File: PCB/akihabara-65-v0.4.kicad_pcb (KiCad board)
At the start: 2 copper layers, 327.6 x 99 mm, 198 parts, among them J1 JST-SH, J2 SWD, Q1 2N7002, SW1 TS-1187A-B-A-B, U1 STM32F072C8Tx, U2 XC6206P332MR, Y1 16 MHz

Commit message: added images, updated readme, updated PCB
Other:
- board text added: "+3.3v"
- board text added: "4.5u"
- board text added: "6.25u"
- board text added: "7u"
- board text added: "Akihabara 65 PCB v0.4 22/03/17 K. Takahashi"
- board text added: "SWCLK"
- board text added: "SWDIO"
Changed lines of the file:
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@@
       (drillshape 0)
       (scaleselection 1)
-      (outputdirectory "Production/")
+      (outputdirectory "../Production/")
     )
   )
@@
     (pad "" np_thru_hole circle (at 0 0) (size 3.9878 3.9878) (drill 3.9878) (layers *.Cu *.Mask))
     (pad "" np_thru_hole circle (at 5.08 0 48.0996) (size 1.75 1.75) (drill 1.75) (layers *.Cu *.Mask))
-    (pad "" np_thru_hole circle (at -34.671 6.985) (size 3.048 3.048) (drill 3.048) (layers F&B.Cu *.Mask))
+    (pad "" np_thru_hole circle locked (at -34.671 6.985) (size 3.048 3.048) (drill 3.048) (layers F&B.Cu *.Mask))
     (pad "1" thru_hole circle (at -3.81 -2.54 48.1) (size 2.25 2.25) (drill 1.47) (layers *.Cu "B.Mask")
       (net 91 "C6") (pinfunction "COL") (pintype "passive"))
@@
     (property "Sheetname" "Switch Matrix")
     (attr smd)
-    (fp_text reference "D68" (at -3.707107 0 180) (layer "B.SilkS")
+    (fp_text reference "D68" (at 3.436643 0 180) (layer "B.SilkS")
       (effects (font (size 1 1) (thickness 0.15)) (justify mirror))
     )
@@
   (gr_arc (start 313.292893 179.880393) (mid 314 180.173286) (end 314.292893 180.880393) (layer "Edge.Cuts") (width 0.2))
   (gr_arc (start 203.176707 160.816757) (mid 202.292183 161.562646) (end 201.166552 161.830393) (layer "Edge.Cuts") (width 0.2))
+  (gr_text "Akihabara 65 PCB v0.4 22/03/17 K. Takahashi" (at 170.917892 177.840393) (layer "B.Cu")
+    (effects (font (size 1.5 1.5) (thickness 0.3)) (justify mirror))
+  )
+  (gr_text "4.5u" (at 205.588893 173.83125) (layer "F.SilkS")
+    (effects (font (size 1 1) (thickness 0.15)))
+  )
+  (gr_text "4.5u" (at 136.246893 173.83125) (layer "F.SilkS")
+    (effects (font (size 1 1) (thickness 0.15)))
+  )
+  (gr_text "SWCLK" (at 364.33125 123.98375) (layer "F.SilkS")
+    (effects (font (size 1 1) (thickness 0.15)) (justify right))
+  )
+  (gr_text "6.25u" (at 223.299043 173.83125) (layer "F.SilkS")
+    (effects (font (size 1 1) (thickness 0.15)))
+  )
+  (gr_text "SWDIO" (at 364.33125 126.52375) (layer "F.SilkS")
+    (effects (font (size 1 1) (thickness 0.15)) (justify right))
+  )
+  (gr_text "6.25u" (at 123.299243 173.83125) (layer "F.SilkS")
+    (effects (font (size 1 1) (thickness 0.15)))
+  )
+  (gr_text "7u" (at 128.055393 173.83125) (layer "F.SilkS")
+    (effects (font (size 1 1) (thickness 0.15)))
+  )
+  (gr_text "7u" (at 242.355393 173.83125) (layer "F.SilkS")
+    (effects (font (size 1 1) (thickness 0.15)))
+  )
+  (gr_text "+3.3v" (at 364.33125 129.06375) (layer "F.SilkS")
+    (effects (font (size 1 1) (thickness 0.15)) (justify right))
+  )
+  (gr_text "Akihabara 65 PCB v0.4 22/03/17 K. Takahashi" (at 170.917892 177.840393) (layer "B.Mask")
+    (effects (font (size 1.5 1.5) (thickness 0.3)) (justify mirror))
+  )
   (segment (start 356.005393 139.255393) (end 356.205393 139.055393) (width 0.8) (layer "F.Cu") (net 1))
   (segment (start 342.75 138.7) (end 343.755393 139.705393) (width 0.8) (layer "F.Cu") (net 1))

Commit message: PCB update
Added bottom row indicators on silkscreen.
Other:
- board text added: "Akihabara 65 PCB v0.4 22/03/21 K. Takahashi"
- board text added: "※"
- board text added: "※ - 4.5u □ - 6.25u △ - 7u"
- board text added: "※ □"
- board text added: "□"
- board text added: "□ △"
- board text added: "△"
- board text removed: "4.5u"
- board text removed: "6.25u"
- board text removed: "7u"
- board text removed: "Akihabara 65 PCB v0.4 22/03/17 K. Takahashi"

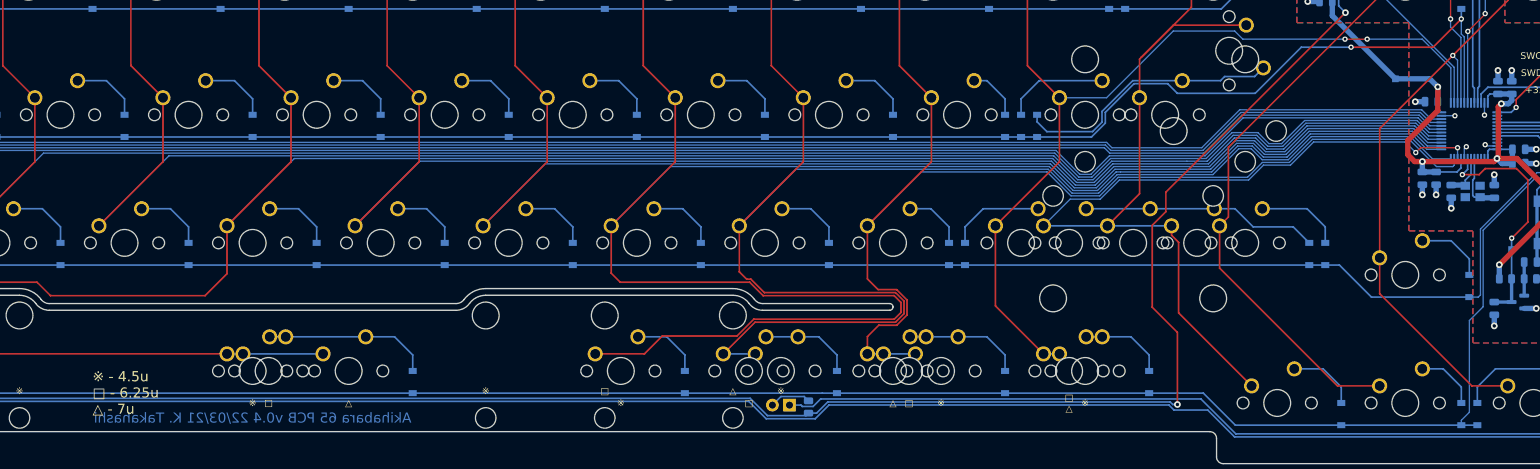
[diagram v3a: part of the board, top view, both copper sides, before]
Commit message: PCB changes, readme, case files now added
- Changed MCU footprint from LQFP-48 to LQFP-48 + UFQFPN-48 dual footprint to combat MCU shortage
- PCB production files are for STM32F072CBUx; edit BOM, CPL, and paste layer if you want SMT assembly for an STM32F072CBTx
- STEP files and their associated technical drawings are now included for the case and plate
- Added more images, updated existing images
- Updated readme
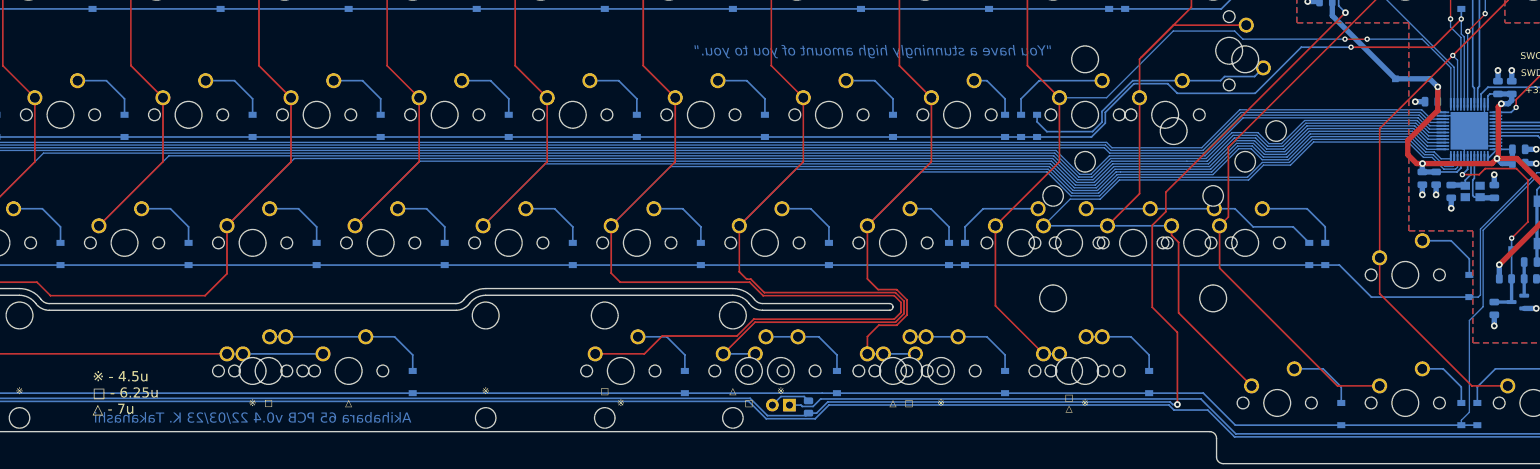
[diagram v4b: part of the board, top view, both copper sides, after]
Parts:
- C8, C9: value 15pF -> 22pF
- U1: value STM32F072C8Tx -> STM32F072CBUx; footprint Package_QFP:LQFP-48_7x7mm_P0.5mm -> Akihabara_Footprints:STM32_CxT_CxU_Hybrid
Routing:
- net GND: track 36.1 -> 44.1 mm, vias 21 -> 17
- net +3V3: track 164.7 -> 164.0 mm
- net C13: track 205.6 -> 206.0 mm, vias 2 -> 0
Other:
- board text added: "+"
- board text added: "Akihabara 65 PCB v0.4 22/03/23 K. Takahashi"
- board text added: "{dblquote}You have a stunningly high amount of you to you.{dblquote}"
- board text removed: "Akihabara 65 PCB v0.4 22/03/21 K. Takahashi"

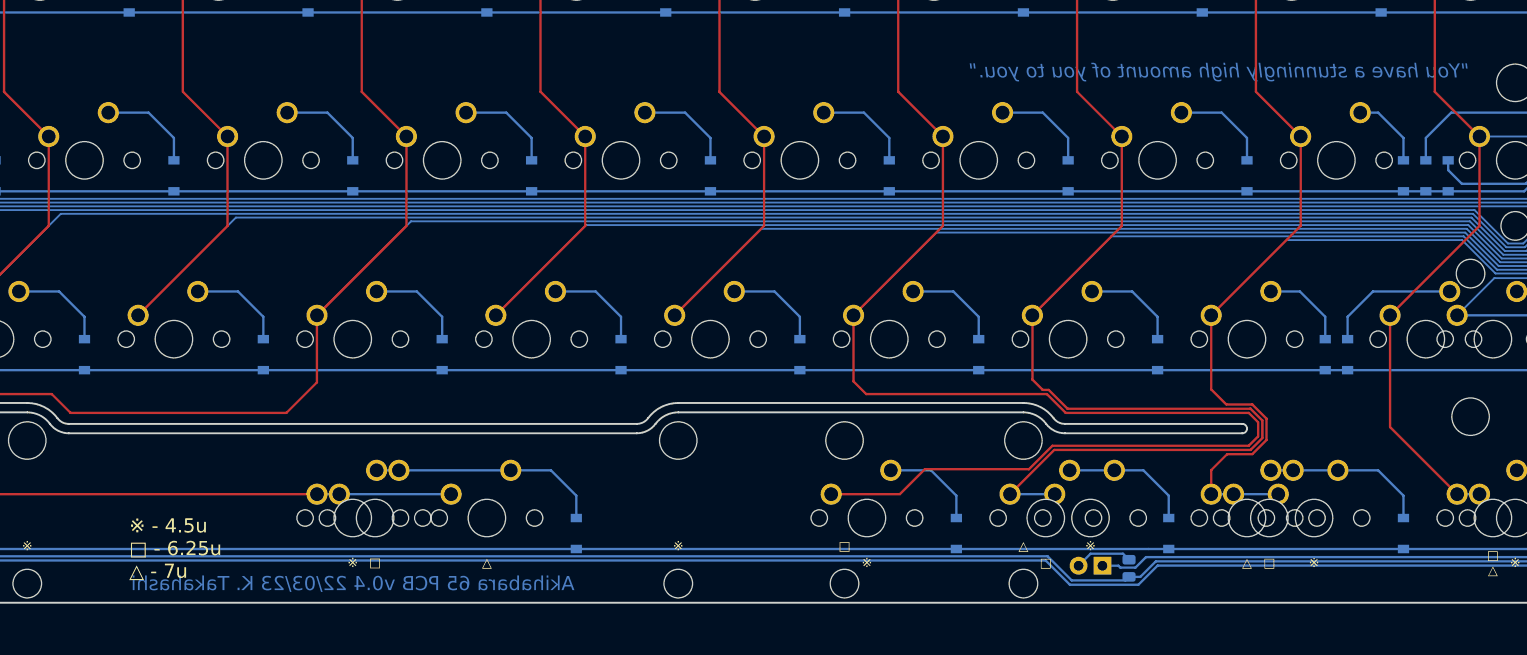
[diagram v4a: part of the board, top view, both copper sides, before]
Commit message: update PCB text
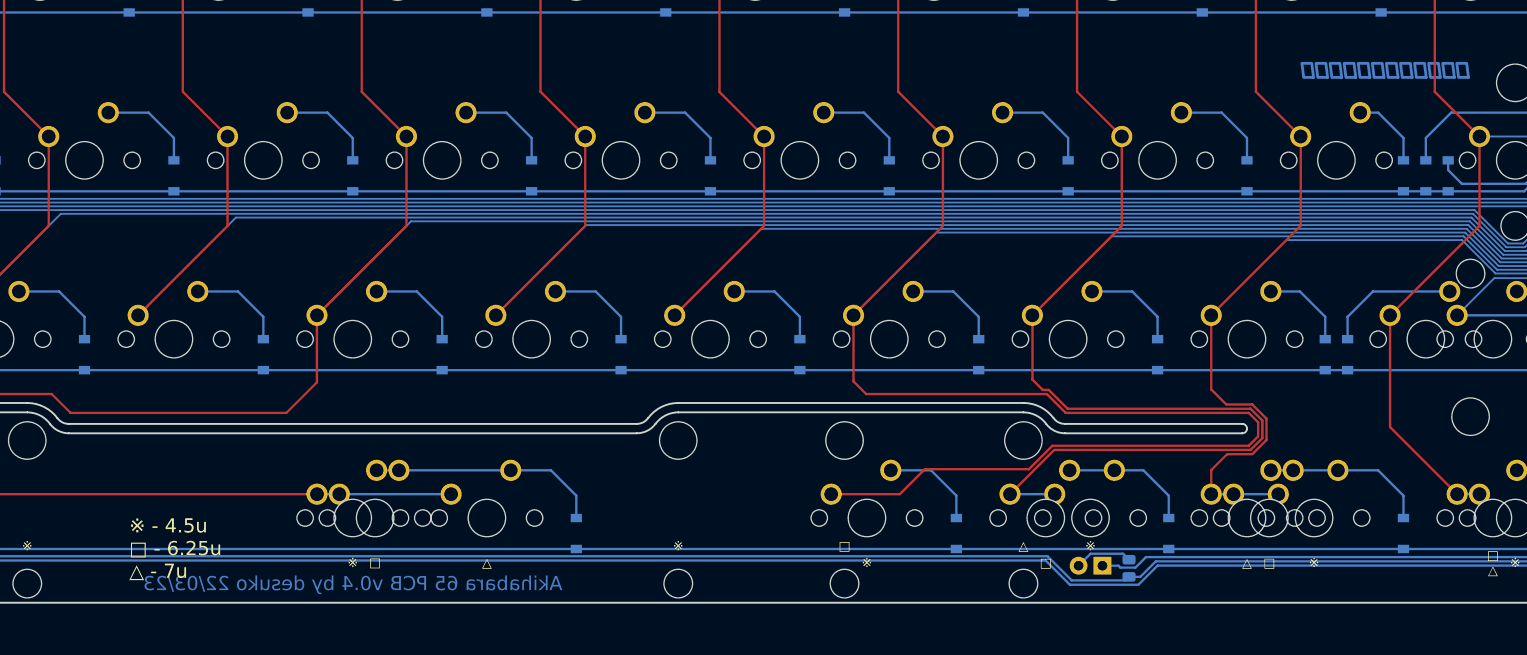
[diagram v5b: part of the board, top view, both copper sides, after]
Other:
- board text added: "Akihabara 65 PCB v0.4 by desuko 22/03/23"
- board text added: "「もう一回、もう一回！」"
- board text removed: "Akihabara 65 PCB v0.4 22/03/23 K. Takahashi"
- board text removed: "{dblquote}You have a stunningly high amount of you to you.{dblquote}"
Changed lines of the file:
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@@
   (gr_arc (start 313.292893 179.880393) (mid 314 180.173286) (end 314.292893 180.880393) (layer "Edge.Cuts") (width 0.2))
   (gr_arc (start 203.176707 160.816757) (mid 202.292183 161.562646) (end 201.166552 161.830393) (layer "Edge.Cuts") (width 0.2))
-  (gr_text "Akihabara 65 PCB v0.4 22/03/23 K. Takahashi" (at 170.917892 177.840393) (layer "B.Cu")
+  (gr_text "Akihabara 65 PCB v0.4 by desuko 22/03/23" (at 170.917892 177.840393) (layer "B.Cu")
     (effects (font (size 1.5 1.5) (thickness 0.3)) (justify mirror))
   )
-  (gr_text "{dblquote}You have a stunningly high amount of you to you.{dblquote}" (at 289.980393 123.230393) (layer "B.Cu")
+  (gr_text "「もう一回、もう一回！」" (at 289.980393 123.230393) (layer "B.Cu")
     (effects (font (size 1.5 1.5) (thickness 0.3) italic) (justify left mirror))
   )
@@
     (effects (font (size 1 1) (thickness 0.15)))
   )
-  (gr_text "Akihabara 65 PCB v0.4 22/03/23 K. Takahashi" (at 170.917892 177.840393) (layer "B.Mask")
+  (gr_text "Akihabara 65 PCB v0.4 by desuko 22/03/23" (at 170.917892 177.840393) (layer "B.Mask")
     (effects (font (size 1.5 1.5) (thickness 0.3)) (justify mirror))
   )
-  (gr_text "{dblquote}You have a stunningly high amount of you to you.{dblquote}" (at 289.980393 123.230393) (layer "B.Mask")
+  (gr_text "「もう一回、もう一回！」" (at 289.980393 123.230393) (layer "B.Mask")
     (effects (font (size 1.5 1.5) (thickness 0.3) italic) (justify left mirror))
   )
